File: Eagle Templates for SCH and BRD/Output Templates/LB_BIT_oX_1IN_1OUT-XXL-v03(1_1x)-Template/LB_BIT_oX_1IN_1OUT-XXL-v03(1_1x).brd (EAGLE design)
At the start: 21.4 x 51.2 mm, 17 parts, among them U1 LV321SOT23-5, U2 LV321SOT23-5

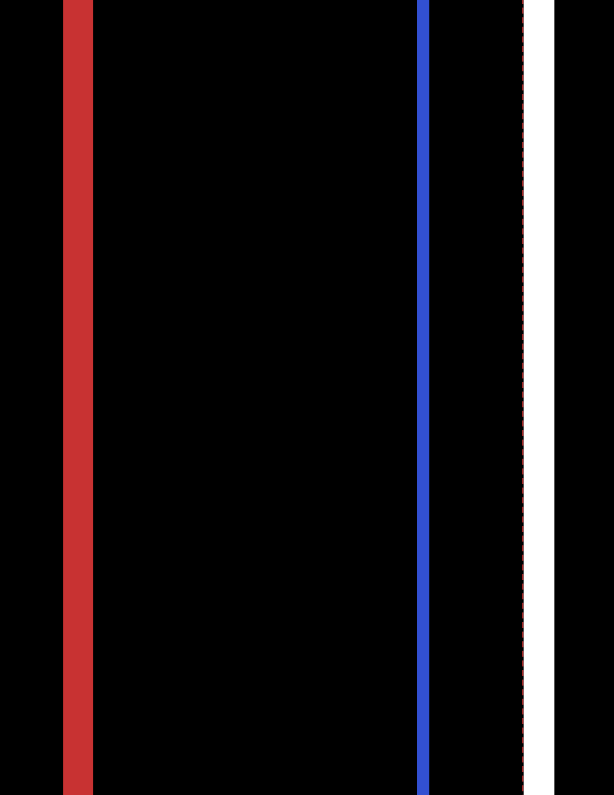
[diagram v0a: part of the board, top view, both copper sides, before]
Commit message: added bitlab logo and made minor changes to board templates. Updated littlebits library.
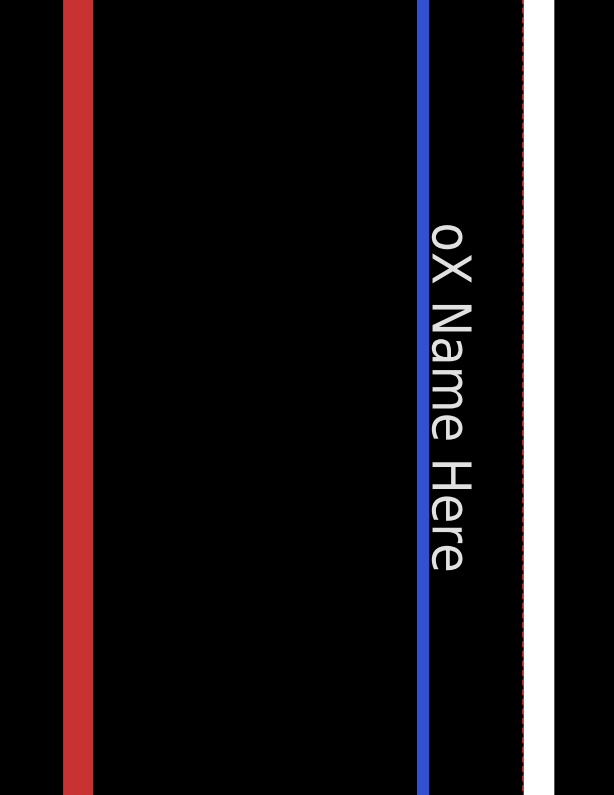
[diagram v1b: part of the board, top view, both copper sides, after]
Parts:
- added U$5: (no value), LITTLEBITS:BITLAB-LOGO
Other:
- board text added: "oX Name Here"
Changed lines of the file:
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@@
 <layer number="111" name="LB_TEXT" color="13" fill="1" visible="yes" active="yes"/>
 <layer number="112" name="tSilk" color="7" fill="1" visible="yes" active="yes"/>
+<layer number="113" name="ReferenceLS" color="7" fill="1" visible="no" active="yes"/>
 <layer number="116" name="Patch_BOT" color="9" fill="4" visible="yes" active="yes"/>
+<layer number="118" name="Rect_Pads" color="7" fill="1" visible="no" active="yes"/>
 <layer number="121" name="_tsilk" color="7" fill="1" visible="yes" active="yes"/>
 <layer number="122" name="_bsilk" color="7" fill="1" visible="yes" active="yes"/>
@@
 <wire x1="2.51" y1="4.11" x2="2.51" y2="55.335" width="1" layer="46"/>
 <wire x1="4.51" y1="55.335" x2="2.51" y2="55.335" width="1" layer="46"/>
+<text x="21" y="29.8" size="1.3" layer="21" font="vector" rot="SR270" align="center">oX Name Here</text>
 </plain>
 <attributes>
@@
 <element name="U$4" library="ohw-logo" package="OSHW_FILLX150_NOTEXT" value="" x="19" y="49.9" rot="MR90"/>
 <element name="U$1" library="LITTLEBITS" package="FABDWG01-OHW" value="FRAME-LETTER" x="0" y="0"/>
+<element name="U$5" library="LITTLEBITS" package="BITLAB-LOGO" value="" x="19.2" y="34.1" rot="R270"/>
 </elements>
 <signals>

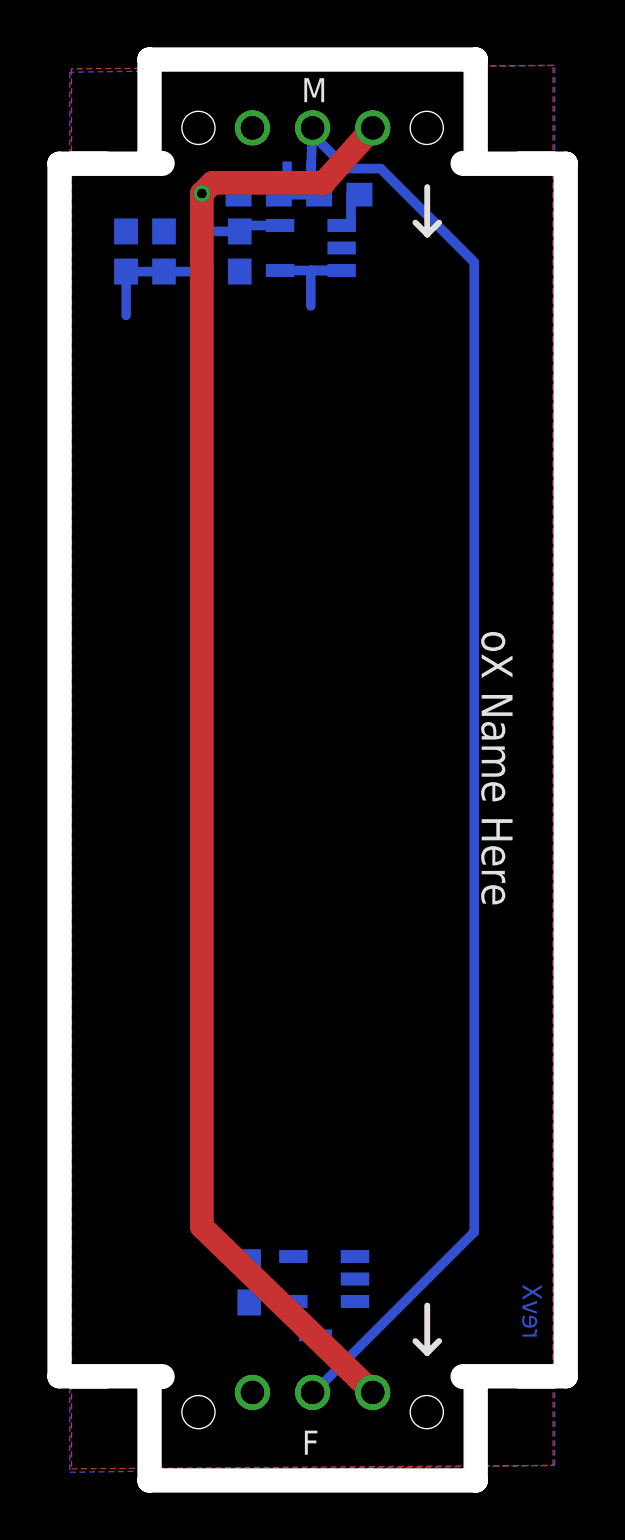
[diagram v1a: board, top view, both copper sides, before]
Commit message: Updated templates
- Added ferrite beads
- Moved text and annotations off of Nets layer
- Minor layout changes
- Removed I/O/W prefix from reference designators
- Removed output stage components from output bits
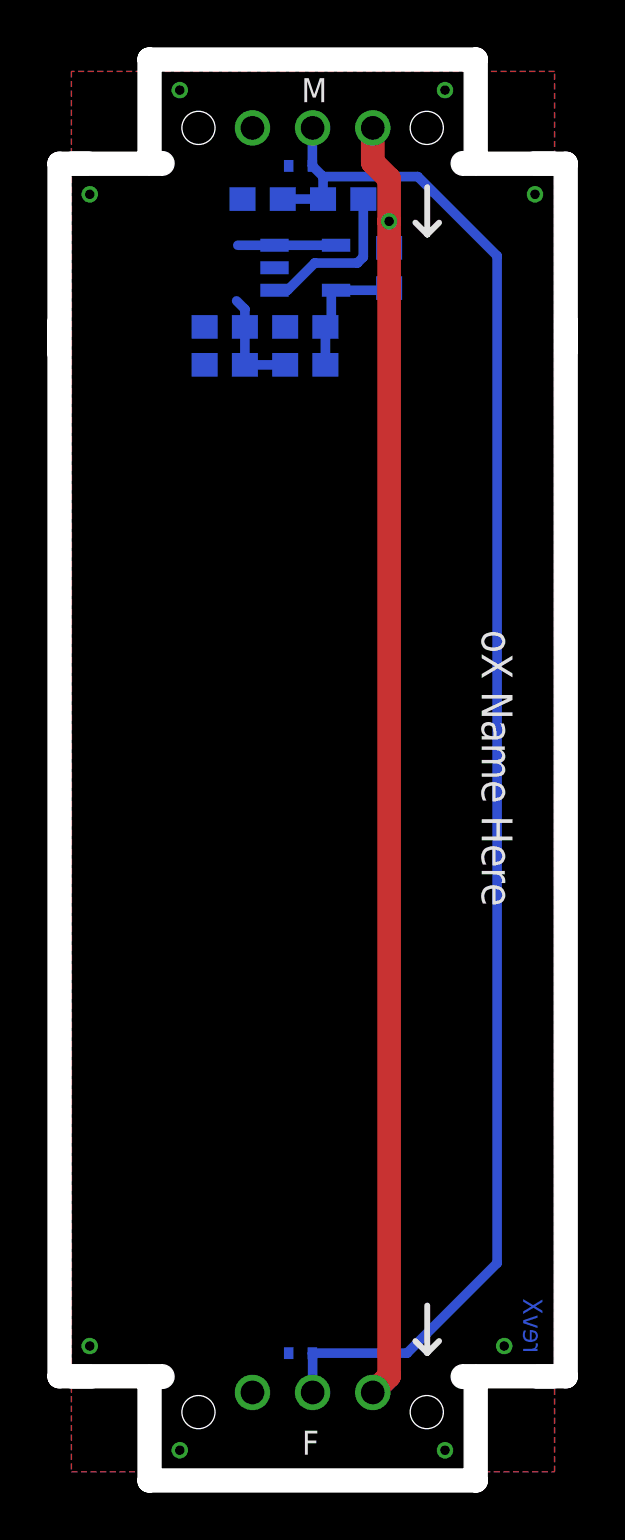
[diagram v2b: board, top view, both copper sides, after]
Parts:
- removed I?C1: 0.1uF, LITTLEBITS:CAP-0603
- removed I?C2: 10uF, LITTLEBITS:CAP-0603
- removed I?C3: 1.0uF, LITTLEBITS:CAP-0603
- removed I?R1: 1meg, LITTLEBITS:RES-0603
- removed I?R2: 10K, LITTLEBITS:RES-0603
- removed I?R3, I?R4: 3K3, LITTLEBITS:RES-0603
- removed I?TVS1, I?TVS2: ESD9B5.0ST5G, LITTLEBITS:SOD-923
- removed U2: LV321SOT23-5, LITTLEBITS:SOT23-5
- added C1: 0.1uF, LITTLEBITS:CAP-0603
- added C2: 10uF, LITTLEBITS:CAP-0603
- added FB1: FERRITE-BEAD0603, LITTLEBITS:R0603
- added R1: 1meg, LITTLEBITS:RES-0603
- added R2: 10K, LITTLEBITS:RES-0603
- added R3, R4: 3K3, LITTLEBITS:RES-0603
- added TVS1, TVS2: ESD9B5.0ST5G, LITTLEBITS:SOD-923
- U$1: value FRAME-LETTER -> OSHW-LOGOL; device LITTLEBITS:FABDWG01-OHW -> LITTLEBITS131206:OSHW-LOGO-L
- U$3: value OSHW-LOGOL -> FRAME-LETTER; device LITTLEBITS131206:OSHW-LOGO-L -> LITTLEBITS:FABDWG01-OHW
- moved U$1 77.8 mm to (-37.5, -68.2)
- moved U$3 75.6 mm to (0.00, 0.00)
- moved U$2 3.45 mm to (-92.2, -64.3)
- moved U1 0.87 mm to (12.9, 50.9), turned to 90 degrees
- renumbered I?BSF to BSF1, I?BSM to BSM1
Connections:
- removed net N$3: U2.1
- removed net SIG_IN: BSF1.SIG, BSM1.SIG1, I?R1.2, I?R2.2, I?TVS1.2
- removed net SIG_OUT: I?TVS2.2, U2.3, U2.4
- new net LB_VCC: BSF1.VCC, BSM1.VCC1, FB1.2
- new net SIG: BSF1.SIG, BSM1.SIG1, R1.2, R2.2, TVS1.2, TVS2.2
- net GND: now also C1.2, C2.2, R1.1, R4.1, TVS1.1, TVS2.1; no longer I?C1.2, I?C2.2, I?C3.1, I?R1.1, I?R4.1, I?TVS1.1, I?TVS2.1, U2.2
- net N$4: now also R2.1; no longer I?R2.1
- net VCC: now also C1.1, FB1.1, R3.2; no longer BSF1.VCC, BSM1.VCC1, I?C1.1, I?C3.2, I?R3.2, U2.5
- net VREF: now also C2.1, R3.1, R4.2; no longer I?C2.1, I?R3.1, I?R4.2
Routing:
- net SIG: track 0.00 -> 67.2 mm
- net SIG_IN: track 65.1 -> 0.00 mm
- net VCC: track 67.3 -> 5.91 mm, vias 1 -> 0
- net LB_VCC: track 0.00 -> 55.1 mm, vias 0 -> 1
- net N$4: track 2.10 -> 6.78 mm
- net N$2: track 5.40 -> 4.15 mm
- net VREF: track 5.05 -> 4.54 mm
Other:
- outline, holes or cut-outs redrawn
